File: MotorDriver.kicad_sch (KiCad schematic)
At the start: 8 parts, among them U2 DRV8434APWPR

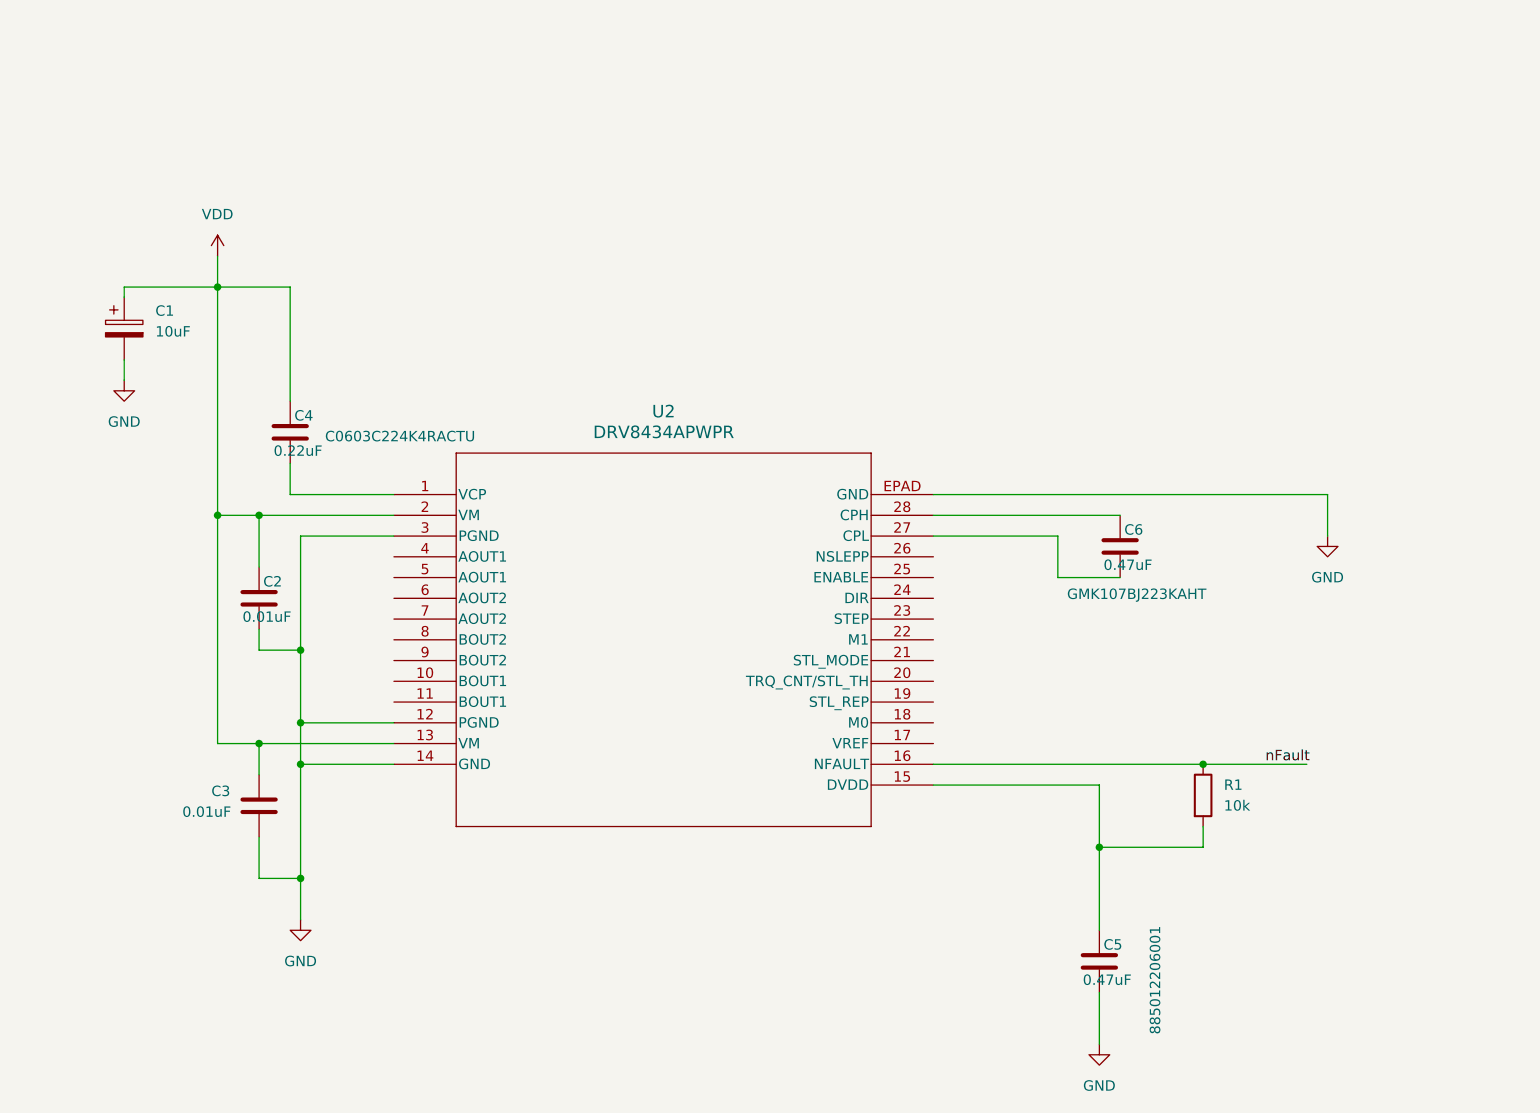
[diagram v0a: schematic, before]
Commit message: Etiquetas y pines modulo driver
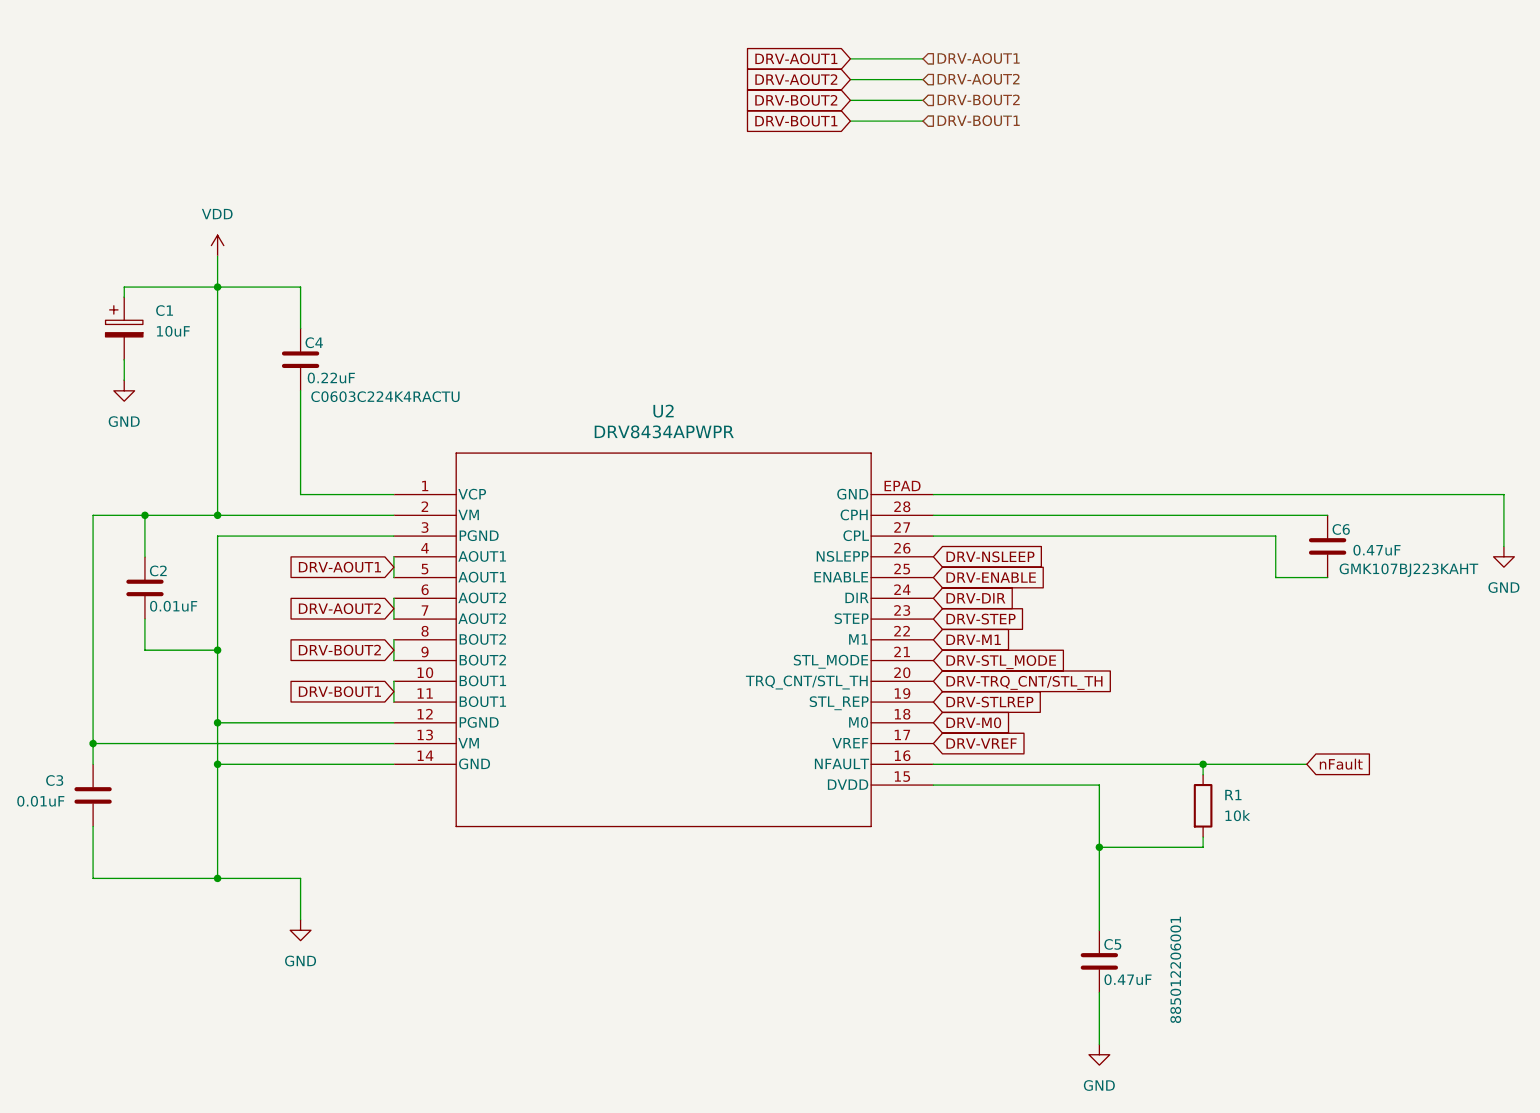
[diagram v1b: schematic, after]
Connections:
- net DRV-BOUT1: now reaches U2.10 (BOUT1)
- net DRV-BOUT1: now also U2.11 (BOUT1)
- net DRV-VREF: now reaches U2.17 (VREF)
- net DRV-M0: now reaches U2.18 (M0)
- net DRV-STLREP: now reaches U2.19 (STL_REP)
- net DRV-TRQ_CNT/STL_TH: now reaches U2.20 (TRQ_CNT/STL_TH)
- net DRV-STL_MODE: now reaches U2.21 (STL_MODE)
- net DRV-M1: now reaches U2.22 (M1)
- net DRV-STEP: now reaches U2.23 (STEP)
- net DRV-DIR: now reaches U2.24 (DIR)
- net DRV-ENABLE: now reaches U2.25 (ENABLE)
- net DRV-NSLEEP: now reaches U2.26 (NSLEPP)
- net DRV-AOUT1: now reaches U2.4 (AOUT1)
- net DRV-AOUT1: now also U2.5 (AOUT1)
- net DRV-AOUT2: now reaches U2.6 (AOUT2)
- net DRV-AOUT2: now also U2.7 (AOUT2)
- net DRV-BOUT2: now reaches U2.8 (BOUT2)
- net DRV-BOUT2: now also U2.9 (BOUT2)
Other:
- moved on the sheet: C2, C3, C4, C6, R1

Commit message: cajetin motor driver actualizado
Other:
- company: (none) -> soft-loop.com
- title: (none) -> drv8434
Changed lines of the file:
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@@
 	(generator_version "8.0")
 	(paper "A4")
+	(title_block
+		(title "drv8434")
+		(date "20/05/2024")
+		(company "soft-loop.com")
+	)
 	(junction
 		(at 200.66 110.49)

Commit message: Schematic done
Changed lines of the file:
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@@
 	)
 	(hierarchical_label "DRV-NFAULT"
-		(shape input)
+		(shape output)
 		(at 196.85 64.77 0)
 		(fields_autoplaced yes)
